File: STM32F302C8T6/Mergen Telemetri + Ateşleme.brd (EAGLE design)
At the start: 49.7 x 87.5 mm, 99 parts, among them J2 U.FL, Q2 IRLML6344TRPBF, Q3 IRLML6344TRPBF, U1 AMS1117-3.3, U2 BMP280, U3 MPU-6050, U4 L86, U6 AMS1117-3.3, U7 AMS1117-3.3, U8 STM32F302C8T6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

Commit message: Regulator name was changed as 5.0
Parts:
- U1, U7: value AMS1117-3.3 -> AMS1117-5.0
- moved C4 46.4 mm to (2.34, 33.0), flipped to the bottom
- moved STM 45.0 mm to (48.0, 65.4), flipped to the top
- moved C6 43.4 mm to (3.81, 37.9), flipped to the bottom
- moved C3 43.4 mm to (3.84, 42.0), flipped to the bottom
- moved X1 43.3 mm to (47.2, 35.7), flipped to the top
- moved B2 40.8 mm to (45.9, 71.4), flipped to the top
- moved SW1 40.7 mm to (5.16, 49.9), flipped to the top
- moved POWER 40.6 mm to (5.21, 57.7), flipped to the top
- moved MAIN 40.5 mm to (45.8, 47.1), flipped to the top
- moved APOGEE 40.3 mm to (45.7, 54.9), flipped to the top
- moved J2 39.8 mm to (5.62, 73.1), flipped to the top
- moved X4 39.6 mm to (45.3, 6.65), flipped to the top
- moved F1 39.0 mm to (6.05, 33.3), flipped to the bottom
- moved U6 38.2 mm to (6.45, 63.8), flipped to the bottom
- moved C29 33.9 mm to (8.59, 26.4), flipped to the bottom
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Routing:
- added copper zone on layer 16, net HT
- added copper zone on layer 16, net HT2
- added copper zone on layer 16, net HT3
- removed copper zone on layer 1, net HT
- removed copper zone on layer 1, net HT2
- removed copper zone on layer 1, net HT3
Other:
- outline, holes or cut-outs redrawn
- board text added: "3.3"
- board text added: "CLK"
- board text added: "GND"
- board text added: "IO"
- board text added: "RX3"
- board text added: "TX3"

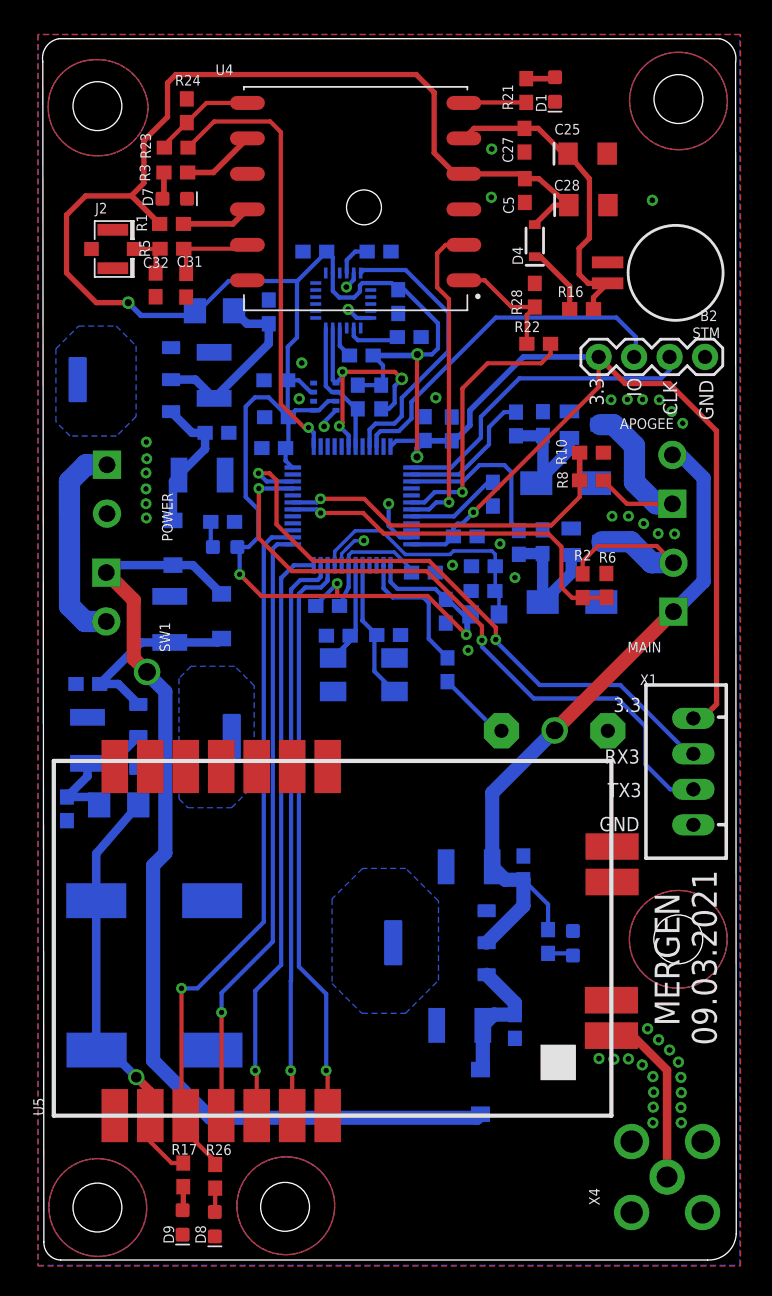
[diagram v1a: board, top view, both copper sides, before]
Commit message: last updates was completed, Ready for flying
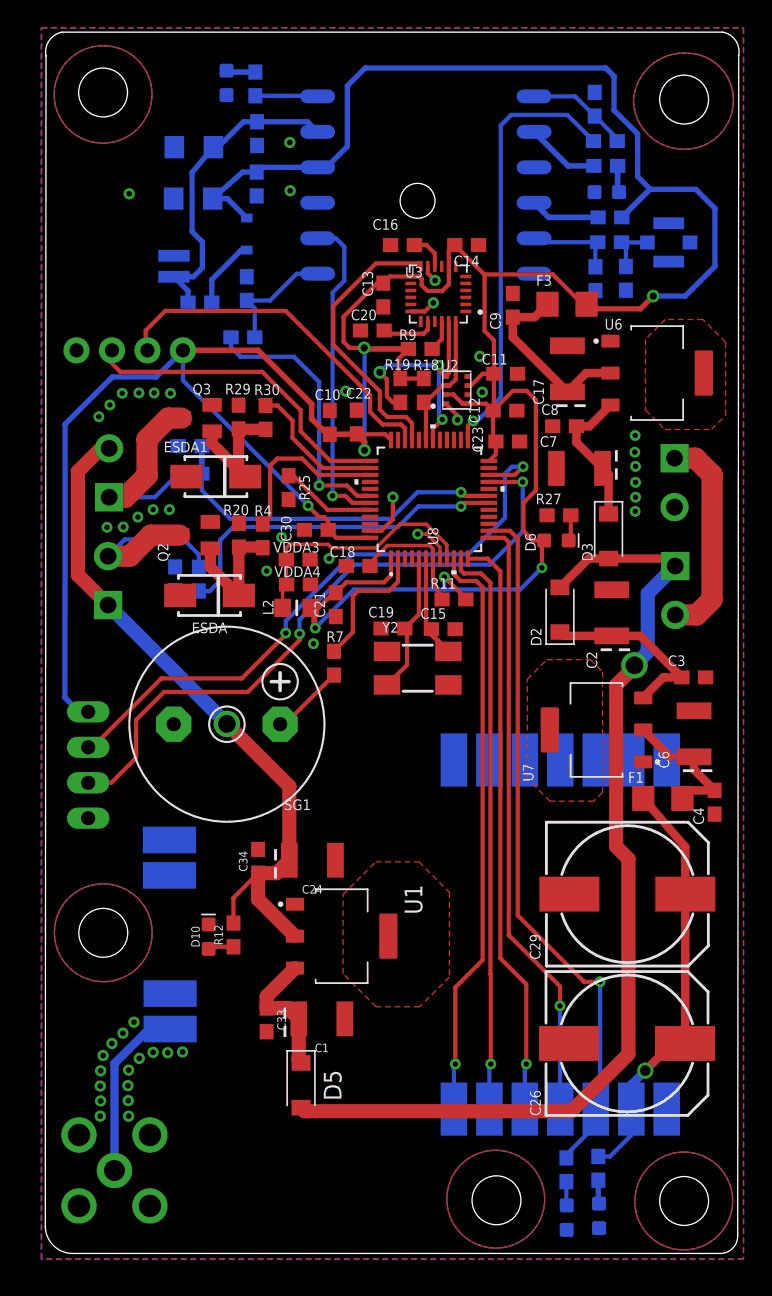
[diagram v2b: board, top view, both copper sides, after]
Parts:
- moved C4 46.4 mm to (48.7, 33.5), flipped to the top
- moved STM 45.0 mm to (3.02, 65.8), flipped to the bottom
- moved C6 43.4 mm to (47.2, 38.4), flipped to the top
- moved C3 43.4 mm to (47.2, 42.4), flipped to the top
- moved X1 43.3 mm to (3.86, 36.2), flipped to the bottom
- moved B2 40.8 mm to (5.13, 71.9), flipped to the bottom
- moved SW1 40.7 mm to (45.9, 50.4), flipped to the bottom
- moved POWER 40.6 mm to (45.8, 58.1), flipped to the bottom
- moved MAIN 40.5 mm to (5.28, 47.6), flipped to the bottom
- moved APOGEE 40.3 mm to (5.36, 55.3), flipped to the bottom
- moved J2 39.8 mm to (45.4, 73.6), flipped to the bottom
- moved X4 39.6 mm to (5.74, 7.12), flipped to the bottom
- moved F1 39.0 mm to (45.0, 33.8), flipped to the top
- moved U6 38.2 mm to (44.6, 64.2), flipped to the top
- moved C29 33.9 mm to (42.5, 26.9), flipped to the top
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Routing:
- added copper zone on layer 1, net HT
- added copper zone on layer 1, net HT2
- added copper zone on layer 1, net HT3
- removed copper zone on layer 16, net HT
- removed copper zone on layer 16, net HT2
- removed copper zone on layer 16, net HT3
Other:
- outline, holes or cut-outs redrawn
